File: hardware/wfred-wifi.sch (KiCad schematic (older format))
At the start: 11 parts, among them K401 UART_ESP, K402 UART_AVR, P401 ESP_BOOTLOAD, U401 ESP-12E

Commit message: Take over new keys and new ESP-AVR-connection...
...from other branch
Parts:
- removed R401: 100k, Capacitors_SMD:C_0805_HandSoldering, symbol R-RESCUE-wfred_rev2
- removed R402: 47k, Capacitors_SMD:C_0805_HandSoldering, symbol R-RESCUE-wfred_rev2
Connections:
- net VCC: no longer U401.1 (REST)
- net CLOCK1: no longer names the net of U401.4 (GPIO16)
- net CLOCK2: no longer names the net of U401.5 (GPIO14)
- net LOCO1: no longer names the net of U401.14 (GPIO5)
- net LOCO2: no longer names the net of U401.13 (GPIO4)
- net LOCO3: no longer names the net of U401.6 (GPIO12)
- net LOCO4: no longer names the net of U401.7 (GPIO13)
- no-connect marks 6 -> 14
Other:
- moved on the sheet: C401, C402
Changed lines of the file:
@@
 LIBS:my_devices
 LIBS:ESP8266
+LIBS:LDL1117S30R
+LIBS:MCP73831T-2ACI_OT
+LIBS:NCV8161BSN300T1G
 LIBS:wfred_rev2-cache
 EELAYER 25 0
@@
 	1    0    0    -1
 $EndComp
-$Comp
-L +BATT #PWR036
-U 1 1 5A11AB98
-P 2500 1500
-F 0 "#PWR036" H 2500 1450 20  0001 C CNN
-F 1 "+BATT" H 2500 1600 30  0000 C CNN
-F 2 "" H 2500 1500 60  0001 C CNN
-F 3 "" H 2500 1500 60  0001 C CNN
-	1    2500 1500
-	1    0    0    -1
-$EndComp
-Wire Wire Line
-	2500 1500 2500 1800
-$Comp
-L R-RESCUE-wfred_rev2 R401
-U 1 1 5A11AE00
-P 2500 2050
-F 0 "R401" V 2580 2050 40  0000 C CNN
-F 1 "100k" V 2507 2051 40  0000 C CNN
-F 2 "Capacitors_SMD:C_0805_HandSoldering" V 2430 2050 30  0001 C CNN
-F 3 "" H 2500 2050 30  0000 C CNN
-F 4 "603-RC0805JR-07100KL" V 2500 2050 60  0001 C CNN "Mouser"
-	1    2500 2050
-	1    0    0    -1
-$EndComp
-$Comp
-L R-RESCUE-wfred_rev2 R402
-U 1 1 5A11AE49
-P 2500 2750
-F 0 "R402" V 2580 2750 40  0000 C CNN
-F 1 "47k" V 2507 2751 40  0000 C CNN
-F 2 "Capacitors_SMD:C_0805_HandSoldering" V 2430 2750 30  0001 C CNN
-F 3 "" H 2500 2750 30  0000 C CNN
-F 4 "603-RC0805JR-07100KL" V 2500 2750 60  0001 C CNN "Mouser"
-	1    2500 2750
-	1    0    0    -1
-$EndComp
-Wire Wire Line
-	2500 2300 2500 2500
-Wire Wire Line
-	3400 2400 2500 2400
-Connection ~ 2500 2400
-$Comp
-L GND-RESCUE-wfred_rev2 #PWR037
-U 1 1 5A11B098
-P 2500 3700
-F 0 "#PWR037" H 2500 3700 30  0001 C CNN
-F 1 "GND" H 2500 3630 30  0001 C CNN
-F 2 "" H 2500 3700 60  0001 C CNN
-F 3 "" H 2500 3700 60  0001 C CNN
-	1    2500 3700
-	1    0    0    -1
-$EndComp
-Wire Wire Line
-	2500 3700 2500 3000
 NoConn ~ 4050 3500
 NoConn ~ 4150 3500
@@
 NoConn ~ 4550 3500
 $Comp
-L VCC #PWR038
+L VCC #PWR039
 U 1 1 5A11E004
 P 2700 1500
-F 0 "#PWR038" H 2700 1600 30  0001 C CNN
+F 0 "#PWR039" H 2700 1600 30  0001 C CNN
 F 1 "VCC" H 2700 1600 30  0000 C CNN
 F 2 "" H 2700 1500 60  0001 C CNN
@@
 	2700 1500 2700 3000
 Wire Wire Line
-	2700 2300 3400 2300
-Wire Wire Line
 	2700 3000 3400 3000
-Connection ~ 2700 2300
 Wire Wire Line
 	3400 2500 2700 2500
 Connection ~ 2700 2500
 $Comp
-L GND-RESCUE-wfred_rev2 #PWR039
+L GND-RESCUE-wfred_rev2 #PWR040
 U 1 1 5A11E30D
 P 6700 3700
-F 0 "#PWR039" H 6700 3700 30  0001 C CNN
+F 0 "#PWR040" H 6700 3700 30  0001 C CNN
 F 1 "GND" H 6700 3630 30  0001 C CNN
 F 2 "" H 6700 3700 60  0001 C CNN
@@
 Connection ~ 6700 3000
 $Comp
-L VCC #PWR040
+L VCC #PWR041
 U 1 1 5A11E4AA
 P 6300 1550
-F 0 "#PWR040" H 6300 1650 30  0001 C CNN
+F 0 "#PWR041" H 6300 1650 30  0001 C CNN
 F 1 "VCC" H 6300 1650 30  0000 C CNN
 F 2 "" H 6300 1550 60  0001 C CNN
@@
 	5200 2700 6750 2700
 $Comp
-L GND-RESCUE-wfred_rev2 #PWR041
+L GND-RESCUE-wfred_rev2 #PWR042
 U 1 1 5A11FC27
 P 7850 2500
-F 0 "#PWR041" H 7850 2500 30  0001 C CNN
+F 0 "#PWR042" H 7850 2500 30  0001 C CNN
 F 1 "GND" H 7850 2430 30  0001 C CNN
 F 2 "" H 7850 2500 60  0001 C CNN
@@
 	6100 2900 6100 3100
 $Comp
-L GND-RESCUE-wfred_rev2 #PWR042
+L GND-RESCUE-wfred_rev2 #PWR043
 U 1 1 5A120E87
 P 6100 3700
-F 0 "#PWR042" H 6100 3700 30  0001 C CNN
+F 0 "#PWR043" H 6100 3700 30  0001 C CNN
 F 1 "GND" H 6100 3630 30  0001 C CNN
 F 2 "" H 6100 3700 60  0001 C CNN
@@
 	6750 2900 6700 2900
 Connection ~ 6700 2900
-Text GLabel 5400 2500 2    60   Input ~ 0
-LOCO1
-Text GLabel 5400 2600 2    60   Input ~ 0
-LOCO2
-Text GLabel 3200 2800 0    60   Input ~ 0
-LOCO3
-Text GLabel 3200 2900 0    60   Input ~ 0
-LOCO4
-Text GLabel 3200 2600 0    60   Output ~ 0
-CLOCK1
-Text GLabel 3200 2700 0    60   Output ~ 0
-CLOCK2
-Wire Wire Line
-	3200 2600 3400 2600
-Wire Wire Line
-	3400 2700 3200 2700
-Wire Wire Line
-	3400 2800 3200 2800
-Wire Wire Line
-	3200 2900 3400 2900
-Wire Wire Line
-	5200 2500 5400 2500
-Wire Wire Line
-	5400 2600 5200 2600
 $Comp
 L C-RESCUE-wfred_rev2 C401
 U 1 1 5A127BCA
-P 1400 2400
+P 1200 2400
 AR Path="/5A127BCA" Ref="C401"  Part="1"
 AR Path="/5A122619/5A127BCA" Ref="C401"  Part="1"
-F 0 "C401" H 1400 2500 40  0000 L CNN
-F 1 "100n" H 1406 2315 40  0000 L CNN
-F 2 "Capacitors_SMD:C_0805_HandSoldering" H 1438 2250 30  0001 C CNN
-F 3 "" H 1400 2400 60  0000 C CNN
-F 4 "X7R-G0805 100N" H 1400 2400 60  0001 C CNN "Reichelt"
-	1    1400 2400
-	1    0    0    -1
-$EndComp
-$Comp
-L VCC #PWR043
+F 0 "C401" H 1200 2500 40  0000 L CNN
+F 1 "100n" H 1206 2315 40  0000 L CNN
+F 2 "Capacitors_SMD:C_0805_HandSoldering" H 1238 2250 30  0001 C CNN
+F 3 "" H 1200 2400 60  0000 C CNN
+F 4 "X7R-G0805 100N" H 1200 2400 60  0001 C CNN "Reichelt"
+	1    1200 2400
+	1    0    0    -1
+$EndComp
+$Comp
+L VCC #PWR044
 U 1 1 5A127C0E
-P 1400 1800
-F 0 "#PWR043" H 1400 1900 30  0001 C CNN
-F 1 "VCC" H 1400 1900 30  0000 C CNN
-F 2 "" H 1400 1800 60  0001 C CNN
-F 3 "" H 1400 1800 60  0001 C CNN
-	1    1400 1800
-	1    0    0    -1
-$EndComp
-Wire Wire Line
-	1400 1800 1400 2200
-$Comp
-L GND-RESCUE-wfred_rev2 #PWR044
+P 1200 1800
+F 0 "#PWR044" H 1200 1900 30  0001 C CNN
+F 1 "VCC" H 1200 1900 30  0000 C CNN
+F 2 "" H 1200 1800 60  0001 C CNN
+F 3 "" H 1200 1800 60  0001 C CNN
+	1    1200 1800
+	1    0    0    -1
+$EndComp
+Wire Wire Line
+	1200 1800 1200 2200
+$Comp
+L GND-RESCUE-wfred_rev2 #PWR045
 U 1 1 5A127CDB
-P 1400 2900
-F 0 "#PWR044" H 1400 2900 30  0001 C CNN
-F 1 "GND" H 1400 2830 30  0001 C CNN
-F 2 "" H 1400 2900 60  0001 C CNN
-F 3 "" H 1400 2900 60  0001 C CNN
-	1    1400 2900
-	1    0    0    -1
-$EndComp
-Wire Wire Line
-	1400 2900 1400 2600
+P 1200 2900
+F 0 "#PWR045" H 1200 2900 30  0001 C CNN
+F 1 "GND" H 1200 2830 30  0001 C CNN
+F 2 "" H 1200 2900 60  0001 C CNN
+F 3 "" H 1200 2900 60  0001 C CNN
+	1    1200 2900
+	1    0    0    -1
+$EndComp
+Wire Wire Line
+	1200 2600 1200 2900
 $Comp
 L C-RESCUE-wfred_rev2 C402
 U 1 1 5A199174
-P 1700 2400
+P 1500 2400
 AR Path="/5A199174" Ref="C402"  Part="1"
 AR Path="/5A122619/5A199174" Ref="C402"  Part="1"
-F 0 "C402" H 1700 2500 40  0000 L CNN
-F 1 "22u" H 1706 2315 40  0000 L CNN
-F 2 "Capacitors_SMD:C_0805_HandSoldering" H 1738 2250 30  0001 C CNN
-F 3 "" H 1700 2400 60  0000 C CNN
-F 4 "X5R-G0805 22/25" H 1700 2400 60  0001 C CNN "Reichelt"
-	1    1700 2400
-	1    0    0    -1
-$EndComp
-Wire Wire Line
-	1400 2000 1700 2000
-Wire Wire Line
-	1700 2000 1700 2200
-Connection ~ 1400 2000
-Wire Wire Line
-	1700 2600 1700 2800
-Wire Wire Line
-	1700 2800 1400 2800
-Connection ~ 1400 2800
+F 0 "C402" H 1500 2500 40  0000 L CNN
+F 1 "22u" H 1506 2315 40  0000 L CNN
+F 2 "Capacitors_SMD:C_0805_HandSoldering" H 1538 2250 30  0001 C CNN
+F 3 "" H 1500 2400 60  0000 C CNN
+F 4 "X5R-G0805 22/25" H 1500 2400 60  0001 C CNN "Reichelt"
+	1    1500 2400
+	1    0    0    -1
+$EndComp
+Wire Wire Line
+	1200 2000 1500 2000
+Wire Wire Line
+	1500 2000 1500 2200
+Connection ~ 1200 2000
+Wire Wire Line
+	1500 2600 1500 2800
+Wire Wire Line
+	1500 2800 1200 2800
+Connection ~ 1200 2800
+NoConn ~ 5200 2500
+NoConn ~ 5200 2600
+NoConn ~ 3400 2600
+NoConn ~ 3400 2700
+NoConn ~ 3400 2800
+NoConn ~ 3400 2900
+NoConn ~ 3400 2400
+NoConn ~ 3400 2300
 $EndSCHEMATC

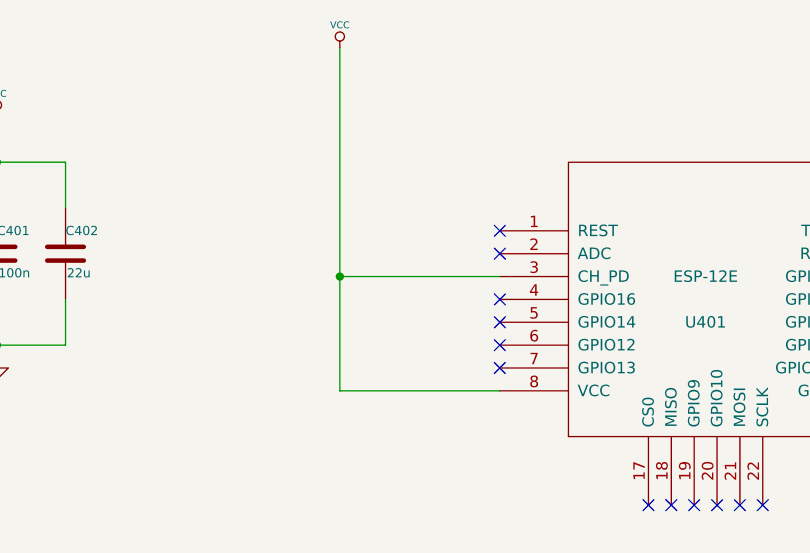
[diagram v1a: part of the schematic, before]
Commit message: Changed schematic to AA batteries and holder
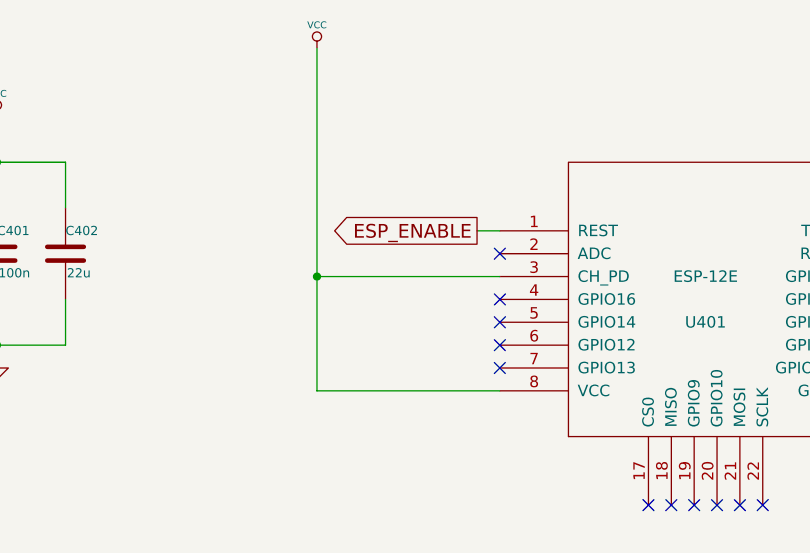
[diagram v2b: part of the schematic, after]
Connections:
- net ESP_ENABLE: now reaches U401.1 (REST)
- no-connect marks 14 -> 13
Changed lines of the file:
@@
 LIBS:my_devices
 LIBS:ESP8266
-LIBS:LDL1117S30R
-LIBS:MCP73831T-2ACI_OT
-LIBS:NCV8161BSN300T1G
 LIBS:wfred_rev2-cache
 EELAYER 25 0
@@
 NoConn ~ 4550 3500
 $Comp
-L VCC #PWR039
+L VCC #PWR026
 U 1 1 5A11E004
-P 2700 1500
-F 0 "#PWR039" H 2700 1600 30  0001 C CNN
-F 1 "VCC" H 2700 1600 30  0000 C CNN
-F 2 "" H 2700 1500 60  0001 C CNN
-F 3 "" H 2700 1500 60  0001 C CNN
-	1    2700 1500
-	1    0    0    -1
-$EndComp
-Wire Wire Line
-	2700 1500 2700 3000
-Wire Wire Line
-	2700 3000 3400 3000
-Wire Wire Line
-	3400 2500 2700 2500
-Connection ~ 2700 2500
-$Comp
-L GND-RESCUE-wfred_rev2 #PWR040
+P 2600 1500
+F 0 "#PWR026" H 2600 1600 30  0001 C CNN
+F 1 "VCC" H 2600 1600 30  0000 C CNN
+F 2 "" H 2600 1500 60  0001 C CNN
+F 3 "" H 2600 1500 60  0001 C CNN
+	1    2600 1500
+	1    0    0    -1
+$EndComp
+Wire Wire Line
+	2600 1500 2600 3000
+Wire Wire Line
+	2600 3000 3400 3000
+Wire Wire Line
+	3400 2500 2600 2500
+Connection ~ 2600 2500
+$Comp
+L GND-RESCUE-wfred_rev2 #PWR027
 U 1 1 5A11E30D
 P 6700 3700
-F 0 "#PWR040" H 6700 3700 30  0001 C CNN
+F 0 "#PWR027" H 6700 3700 30  0001 C CNN
 F 1 "GND" H 6700 3630 30  0001 C CNN
 F 2 "" H 6700 3700 60  0001 C CNN
@@
 Connection ~ 6700 3000
 $Comp
-L VCC #PWR041
+L VCC #PWR028
 U 1 1 5A11E4AA
 P 6300 1550
-F 0 "#PWR041" H 6300 1650 30  0001 C CNN
+F 0 "#PWR028" H 6300 1650 30  0001 C CNN
 F 1 "VCC" H 6300 1650 30  0000 C CNN
 F 2 "" H 6300 1550 60  0001 C CNN
@@
 	5200 2700 6750 2700
 $Comp
-L GND-RESCUE-wfred_rev2 #PWR042
+L GND-RESCUE-wfred_rev2 #PWR029
 U 1 1 5A11FC27
 P 7850 2500
-F 0 "#PWR042" H 7850 2500 30  0001 C CNN
+F 0 "#PWR029" H 7850 2500 30  0001 C CNN
 F 1 "GND" H 7850 2430 30  0001 C CNN
 F 2 "" H 7850 2500 60  0001 C CNN
@@
 	6100 2900 6100 3100
 $Comp
-L GND-RESCUE-wfred_rev2 #PWR043
+L GND-RESCUE-wfred_rev2 #PWR030
 U 1 1 5A120E87
 P 6100 3700
-F 0 "#PWR043" H 6100 3700 30  0001 C CNN
+F 0 "#PWR030" H 6100 3700 30  0001 C CNN
 F 1 "GND" H 6100 3630 30  0001 C CNN
 F 2 "" H 6100 3700 60  0001 C CNN
@@
 $EndComp
 $Comp
-L VCC #PWR044
+L VCC #PWR031
 U 1 1 5A127C0E
 P 1200 1800
-F 0 "#PWR044" H 1200 1900 30  0001 C CNN
+F 0 "#PWR031" H 1200 1900 30  0001 C CNN
 F 1 "VCC" H 1200 1900 30  0000 C CNN
 F 2 "" H 1200 1800 60  0001 C CNN
@@
 	1200 1800 1200 2200
 $Comp
-L GND-RESCUE-wfred_rev2 #PWR045
+L GND-RESCUE-wfred_rev2 #PWR032
 U 1 1 5A127CDB
 P 1200 2900
-F 0 "#PWR045" H 1200 2900 30  0001 C CNN
+F 0 "#PWR032" H 1200 2900 30  0001 C CNN
 F 1 "GND" H 1200 2830 30  0001 C CNN
 F 2 "" H 1200 2900 60  0001 C CNN
@@
 NoConn ~ 3400 2900
 NoConn ~ 3400 2400
-NoConn ~ 3400 2300
+Text GLabel 3300 2300 0    60   Output ~ 0
+ESP_ENABLE
+Wire Wire Line
+	3300 2300 3400 2300
 $EndSCHEMATC
